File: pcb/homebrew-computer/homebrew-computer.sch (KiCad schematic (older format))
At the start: 0 parts

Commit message: Keep working on the peripheral interface
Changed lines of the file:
@@
 $EndDescr
 $Sheet
-S 5450 3650 1250 2200
+S 5450 3650 1200 2200
 U 5F8B5E3D
 F0 "Control Logic" 50
@@
 F20 "DBUS15" I L 5450 5600 50
 F21 "DBUS16" I L 5450 5700 50
-F22 "INSTR_IN" I R 6700 3750 50
-F23 "INSTR_OUT" I R 6700 3850 50
-$EndSheet
-$Sheet
-S 2250 3650 1050 1800
+F22 "INSTR_IN" I R 6650 3750 50
+F23 "INSTR_OUT" I R 6650 3850 50
+$EndSheet
+$Sheet
+S 2250 3650 1200 1800
 U 5F8C07F0
 F0 "Registers" 50
@@
 F16 "DBUS15" B L 2250 5200 50
 F17 "DBUS16" B L 2250 5300 50
-F18 "REG1_IN_L" I R 3300 3800 50
-F19 "REG1_IN_H" I R 3300 3900 50
-F20 "REG1_OUT_L" I R 3300 4000 50
-F21 "REG1_OUT_H" I R 3300 4100 50
-F22 "REG2_IN_L" I R 3300 4250 50
-F23 "REG2_IN_H" I R 3300 4350 50
-F24 "REG2_OUT_L" I R 3300 4450 50
-F25 "REG2_OUT_H" I R 3300 4550 50
-F26 "REG3_IN_L" I R 3300 4700 50
-F27 "REG3_IN_H" I R 3300 4800 50
-F28 "REG3_OUT_L" I R 3300 4900 50
-F29 "REG3_OUT_H" I R 3300 5000 50
-F30 "SP_IN" I R 3300 5150 50
-F31 "SP_OUT" I R 3300 5250 50
+F18 "REG1_IN_L" I R 3450 3800 50
+F19 "REG1_IN_H" I R 3450 3900 50
+F20 "REG1_OUT_L" I R 3450 4000 50
+F21 "REG1_OUT_H" I R 3450 4100 50
+F22 "REG2_IN_L" I R 3450 4250 50
+F23 "REG2_IN_H" I R 3450 4350 50
+F24 "REG2_OUT_L" I R 3450 4450 50
+F25 "REG2_OUT_H" I R 3450 4550 50
+F26 "REG3_IN_L" I R 3450 4700 50
+F27 "REG3_IN_H" I R 3450 4800 50
+F28 "REG3_OUT_L" I R 3450 4900 50
+F29 "REG3_OUT_H" I R 3450 5000 50
+F30 "SP_IN" I R 3450 5150 50
+F31 "SP_OUT" I R 3450 5250 50
 $EndSheet
 $Sheet
@@
 $EndSheet
 $Sheet
-S 1400 3300 550  300
+S 1150 3300 550  300
 U 5F97DC64
 F0 "Clocks" 50
 F1 "clocks.sch" 50
-F2 "CLK" O R 1950 3500 50
-F3 "CLK_I" O R 1950 3400 50
+F2 "CLK" O R 1700 3500 50
+F3 "CLK_I" O R 1700 3400 50
 $EndSheet
 $Sheet
@@
 F32 "ABUS15" B R 6650 2700 50
 F33 "ABUS16" B R 6650 2800 50
-F34 "A_TO_B" I R 6650 2950 50
-F35 "BRIDGE_I" I R 6650 3050 50
-$EndSheet
-$Sheet
-S 3850 1000 1150 2150
+F34 "BRIDGE_I" I R 6650 3050 50
+F35 "A_TO_D" I R 6650 2950 50
+$EndSheet
+$Sheet
+S 3850 3650 1200 2400
+U 5F8B5DB4
+F0 "Peripherals" 50
+F1 "peripherals.sch" 50
+F2 "DBUS1" B L 3850 3800 50
+F3 "DBUS2" B L 3850 3900 50
+F4 "DBUS3" B L 3850 4000 50
+F5 "DBUS4" B L 3850 4100 50
+F6 "DBUS5" B L 3850 4200 50
+F7 "DBUS6" B L 3850 4300 50
+F8 "DBUS7" B L 3850 4400 50
+F9 "DBUS8" B L 3850 4500 50
+F10 "DBUS9" B L 3850 4600 50
+F11 "DBUS10" B L 3850 4700 50
+F12 "DBUS11" B L 3850 4800 50
+F13 "DBUS12" B L 3850 4900 50
+F14 "DBUS13" B L 3850 5000 50
+F15 "DBUS14" B L 3850 5100 50
+F16 "DBUS15" B L 3850 5200 50
+F17 "DBUS16" B L 3850 5300 50
+F18 "ABUS1" B R 5050 3800 50
+F19 "ABUS2" B R 5050 3900 50
+F20 "ABUS3" B R 5050 4000 50
+F21 "ABUS4" B R 5050 4100 50
+F22 "ABUS5" B R 5050 4200 50
+F23 "ABUS6" B R 5050 4300 50
+F24 "ABUS7" B R 5050 4400 50
+F25 "ABUS8" B R 5050 4500 50
+F26 "ABUS9" B R 5050 4600 50
+F27 "ABUS10" B R 5050 4700 50
+F28 "ABUS11" B R 5050 4800 50
+F29 "ABUS12" B R 5050 4900 50
+F30 "ABUS13" B R 5050 5000 50
+F31 "ABUS14" B R 5050 5100 50
+F32 "ABUS15" B R 5050 5200 50
+F33 "ABUS16" B R 5050 5300 50
+F34 "IO_ADDR_IN_I" I R 5050 5450 50
+F35 "INT_OUT_I" I L 3850 5550 50
+F36 "RST_INT" I L 3850 5650 50
+F37 "INT" O L 3850 5450 50
+F38 "IO_OUT_I" I R 5050 5550 50
+F39 "IO_IN_I" I R 5050 5650 50
+F40 "IO_OUTB_I" I R 5050 5800 50
+F41 "IO_INB_I" I R 5050 5900 50
+$EndSheet
+$Sheet
+S 3850 1000 1200 2250
 U 5F95DC76
 F0 "Memory" 50
 F1 "memory.sch" 50
-F2 "DBUS1" B L 3850 1300 50
-F3 "DBUS2" B L 3850 1400 50
-F4 "DBUS3" B L 3850 1500 50
-F5 "DBUS4" B L 3850 1600 50
-F6 "DBUS5" B L 3850 1700 50
-F7 "DBUS6" B L 3850 1800 50
-F8 "DBUS7" B L 3850 1900 50
-F9 "DBUS8" B L 3850 2000 50
-F10 "DBUS9" B L 3850 2100 50
-F11 "DBUS10" B L 3850 2200 50
-F12 "DBUS11" B L 3850 2300 50
-F13 "DBUS12" B L 3850 2400 50
-F14 "DBUS13" B L 3850 2500 50
-F15 "DBUS14" B L 3850 2600 50
-F16 "DBUS15" B L 3850 2700 50
-F17 "DBUS16" B L 3850 2800 50
-F18 "ABUS1" I R 5000 1300 50
-F19 "ABUS2" I R 5000 1400 50
-F20 "ABUS3" I R 5000 1500 50
-F21 "ABUS4" I R 5000 1600 50
-F22 "ABUS5" I R 5000 1700 50
-F23 "ABUS6" I R 5000 1800 50
-F24 "ABUS7" I R 5000 1900 50
-F25 "ABUS8" I R 5000 2000 50
-F26 "ABUS9" I R 5000 2100 50
-F27 "ABUS10" I R 5000 2200 50
-F28 "ABUS11" I R 5000 2300 50
-F29 "ABUS12" I R 5000 2400 50
-F30 "ABUS13" I R 5000 2500 50
-F31 "ABUS14" I R 5000 2600 50
-F32 "ABUS15" I R 5000 2700 50
-F33 "ABUS16" I R 5000 2800 50
-F34 "RAM_OUT_I" I R 5000 2950 50
-F35 "MEM_ADDR_IN_I" I R 5000 3050 50
-$EndSheet
-$Sheet
-S 3850 3650 1150 2150
-U 5F8B5DB4
-F0 "Peripherals" 50
-F1 "peripherals.sch" 50
+F2 "DBUS1" B L 3850 1100 50
+F3 "DBUS2" B L 3850 1200 50
+F4 "DBUS3" B L 3850 1300 50
+F5 "DBUS4" B L 3850 1400 50
+F6 "DBUS5" B L 3850 1500 50
+F7 "DBUS6" B L 3850 1600 50
+F8 "DBUS7" B L 3850 1700 50
+F9 "DBUS8" B L 3850 1800 50
+F10 "DBUS9" B L 3850 1900 50
+F11 "DBUS10" B L 3850 2000 50
+F12 "DBUS11" B L 3850 2100 50
+F13 "DBUS12" B L 3850 2200 50
+F14 "DBUS13" B L 3850 2300 50
+F15 "DBUS14" B L 3850 2400 50
+F16 "DBUS15" B L 3850 2500 50
+F17 "DBUS16" B L 3850 2600 50
+F18 "ABUS1" I R 5050 1100 50
+F19 "ABUS2" I R 5050 1200 50
+F20 "ABUS3" I R 5050 1300 50
+F21 "ABUS4" I R 5050 1400 50
+F22 "ABUS5" I R 5050 1500 50
+F23 "ABUS6" I R 5050 1600 50
+F24 "ABUS7" I R 5050 1700 50
+F25 "ABUS8" I R 5050 1800 50
+F26 "ABUS9" I R 5050 1900 50
+F27 "ABUS10" I R 5050 2000 50
+F28 "ABUS11" I R 5050 2100 50
+F29 "ABUS12" I R 5050 2200 50
+F30 "ABUS13" I R 5050 2300 50
+F31 "ABUS14" I R 5050 2400 50
+F32 "ABUS15" I R 5050 2500 50
+F33 "ABUS16" I R 5050 2600 50
+F34 "RAM_OUT_I" I R 5050 2750 50
+F35 "RAM_ADDR_IN_I" I L 3850 2750 50
+F36 "RAM_IN_I" I R 5050 2850 50
+F37 "RAM_OUTB_I" I R 5050 3000 50
+F38 "RAM_INB_I" I R 5050 3100 50
 $EndSheet
 $EndSCHEMATC

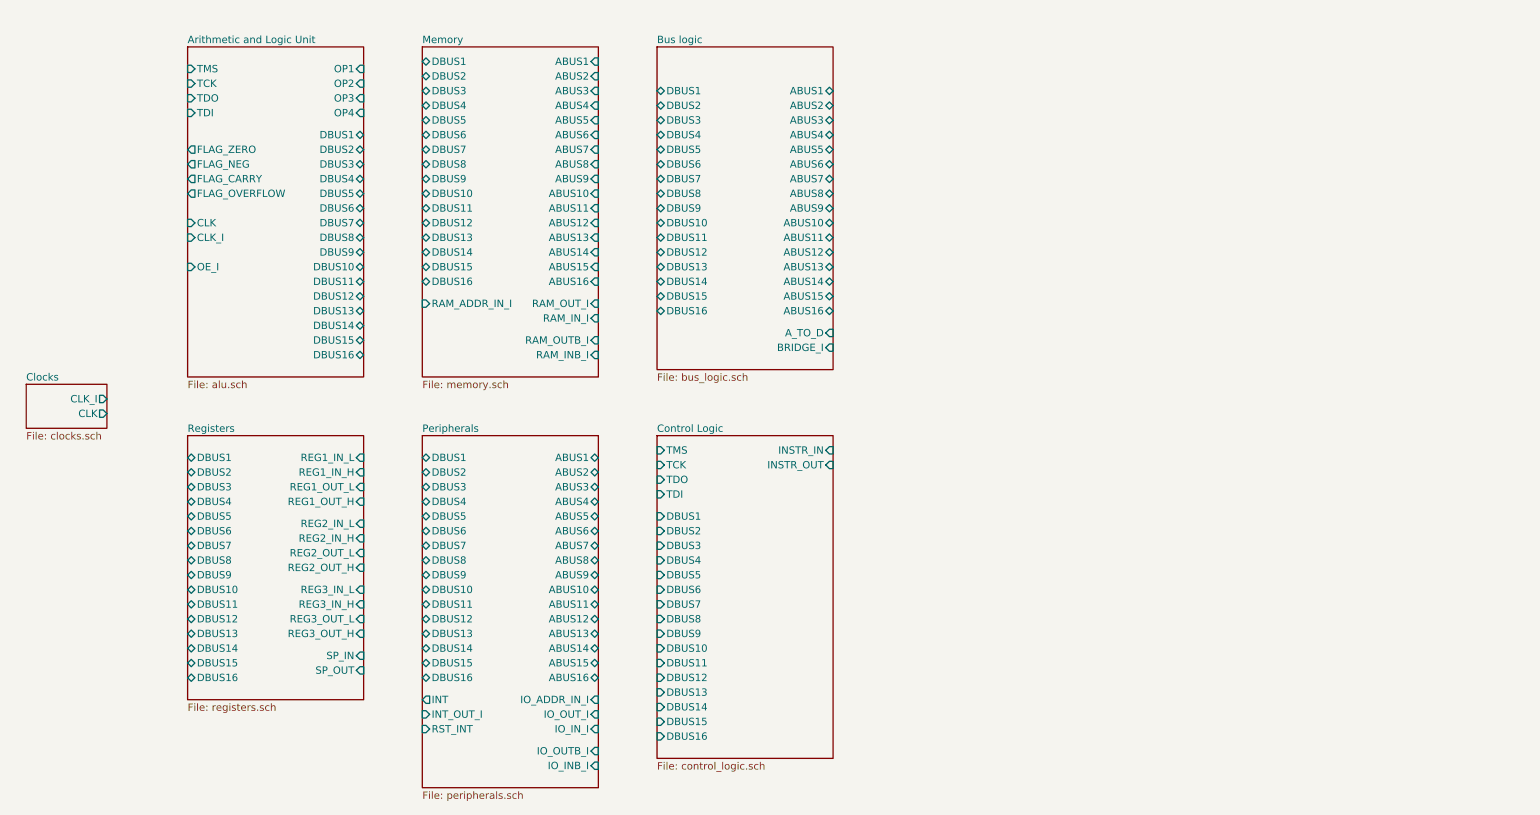
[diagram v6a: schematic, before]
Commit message: Remove the address bus as it would require too big of a connector
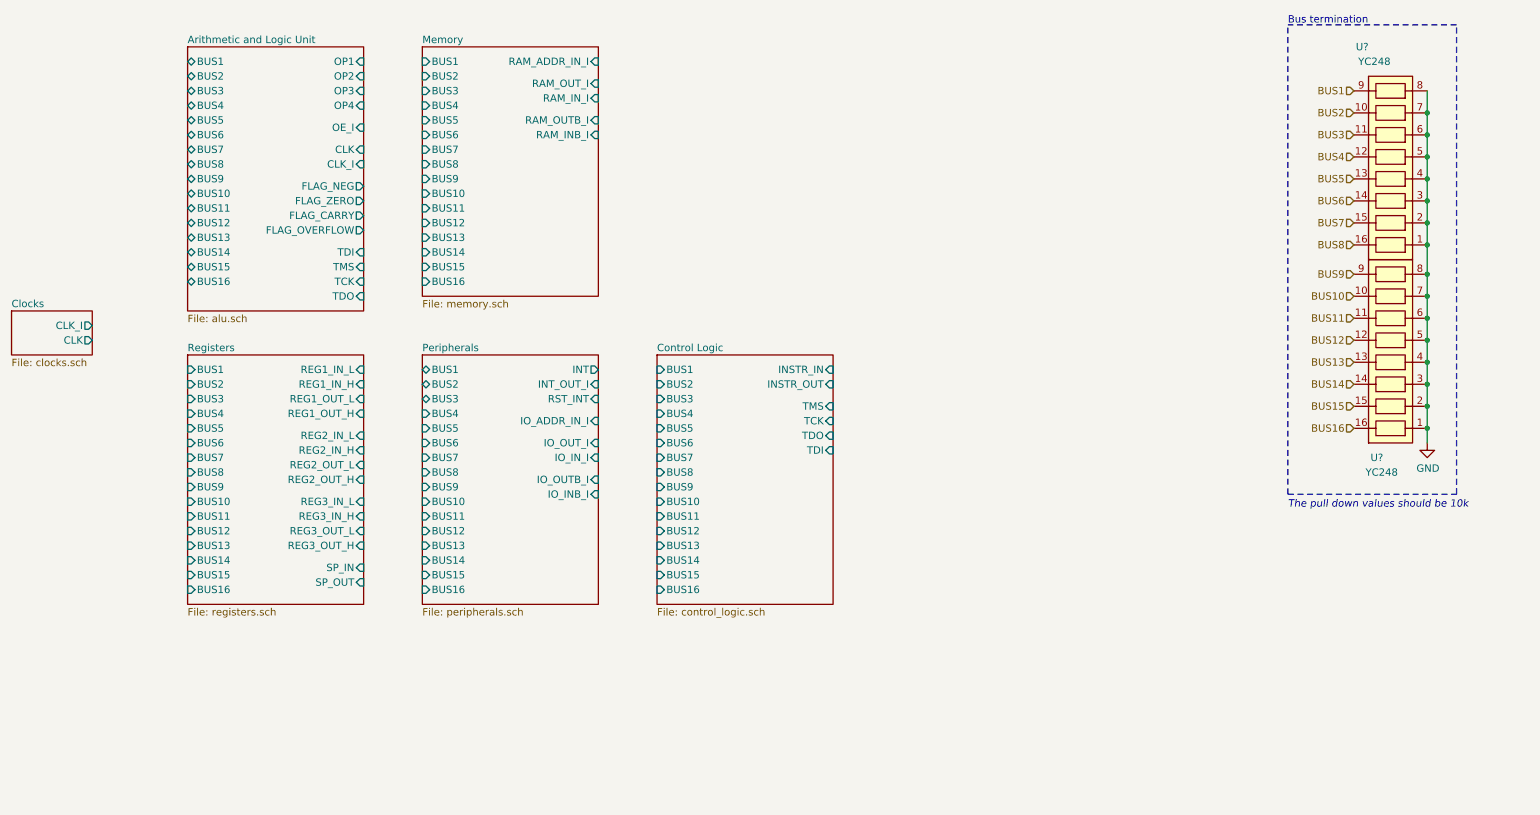
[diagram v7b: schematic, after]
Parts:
- added U? (x2): YC248, symbol YC248:YC248
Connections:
- new net BUS1: U?.9
- new net BUS10: U?.10
- new net BUS11: U?.11
- new net BUS12: U?.12
- new net BUS13: U?.13
- new net BUS14: U?.14
- new net BUS15: U?.15
- new net BUS16: U?.16
- new net BUS2: U?.10
- new net BUS3: U?.11
- new net BUS4: U?.12
- new net BUS5: U?.13
- new net BUS6: U?.14
- new net BUS7: U?.15
- new net BUS8: U?.16
- new net BUS9: U?.9
- new net GND: U?.1, U?.1, U?.2, U?.2, U?.3, U?.3, U?.4, U?.4, U?.5, U?.5, U?.6, U?.6, U?.7, U?.7, U?.8, U?.8
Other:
- note added: "Bus termination"
- note added: "The pull down values should be 10k"

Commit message: Remove unnecessary address bus and unified the IO interface
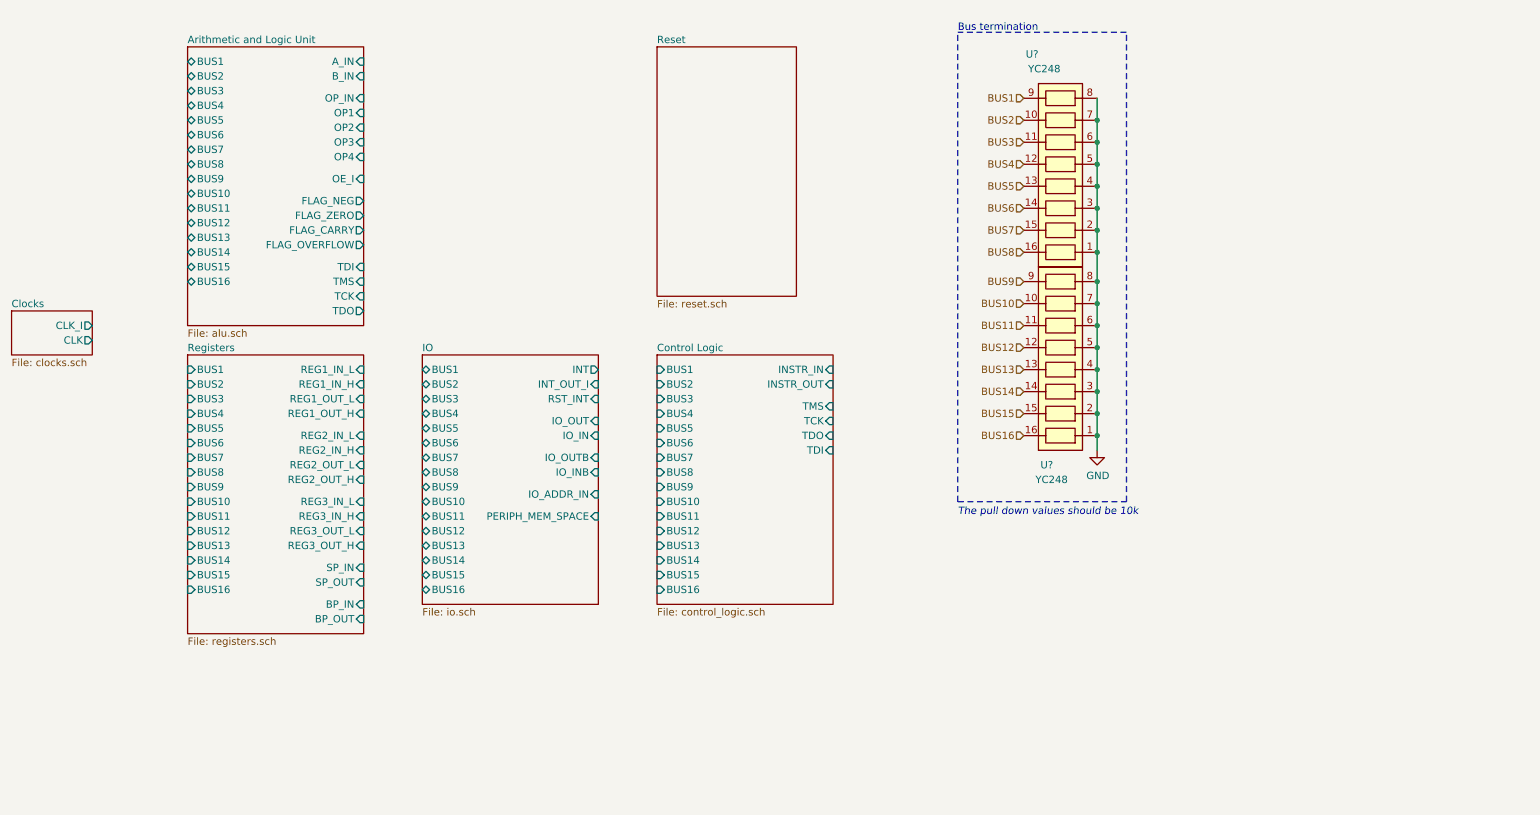
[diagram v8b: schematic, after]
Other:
- moved on the sheet: U?
